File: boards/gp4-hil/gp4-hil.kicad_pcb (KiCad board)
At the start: 4 copper layers, 160 x 62 mm, 450 parts, among them J1 BEL_FUSE_0826-1G1T-23-F, J2 XILINX_JTAG, J3 XILINX_JTAG_ICESIDE, J4 XILINX_JTAG_ICESIDE, K1 CONN_3_PWROUT, P1 GPAK_ZIF, P2 2x10 HEADER, Q1 SSM6N58NU, Q11 SSM6N58NU, Q12 DMP2069UFY4, Q13 SSM6N58NU, Q14 SSM6N58NU, Q15 SSM6N58NU, Q16 SSM6N58NU, Q17 SSM6N58NU, Q18 SSM6N58NU, Q19 SSM6N58NU, Q20 SSM6N58NU, Q21 SSM6N58NU, Q22 DMP2069UFY4, U1 MIC2288-DFN, U10 AD9609, U11 DAC084S085, U12 DAC084S085, U13 DAC084S085, U14 DAC084S085, U15 TS3A4751, U16 TS3A4751, U17 TS3A4751, U18 TS3A4751, U19 TS3A4751, U2 XC7A100T-1FTG256C, U20 SIP32408, U21 SIP32408, U22 SIP32408, U23 SIP32408, U24 SIP32408, U25 TS3A4751, U26 TS3A4751, U27 TS3A4751, U29 TXB0104RUT, U3 LTC3374-QFN, U30 TXB0104RUT, U31 ADA4937-2, U32 SIP32408, U33 125 MHz, U34 INA199A2RSW, U35 INA199A2RSW, U36 INA199A2RSW, U4 SIP32408, U5 KSZ9031RN, U6 W25Q32FW, U7 25 MHz, U8 ADG726, U9 AD9609

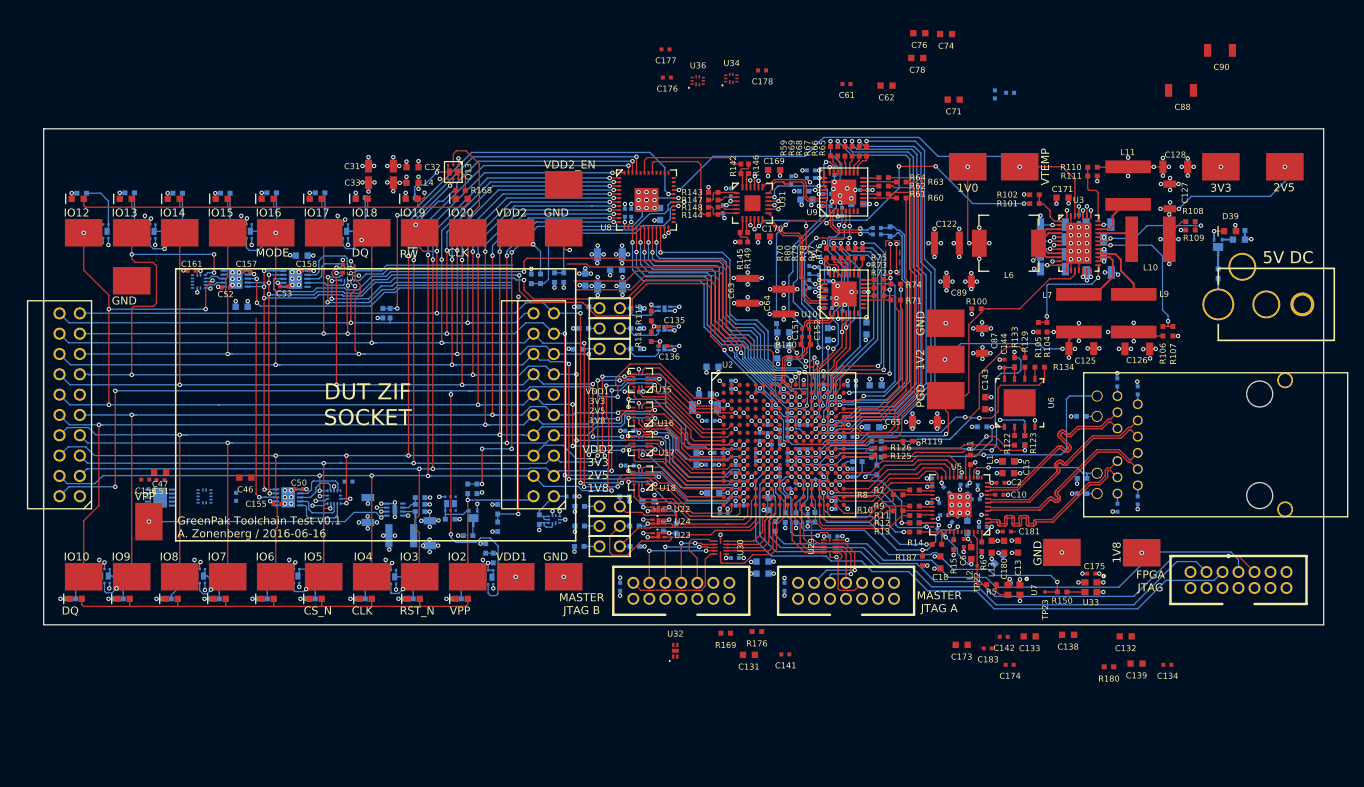
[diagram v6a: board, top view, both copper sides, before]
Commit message: Continued routing test board. 109 nets left.
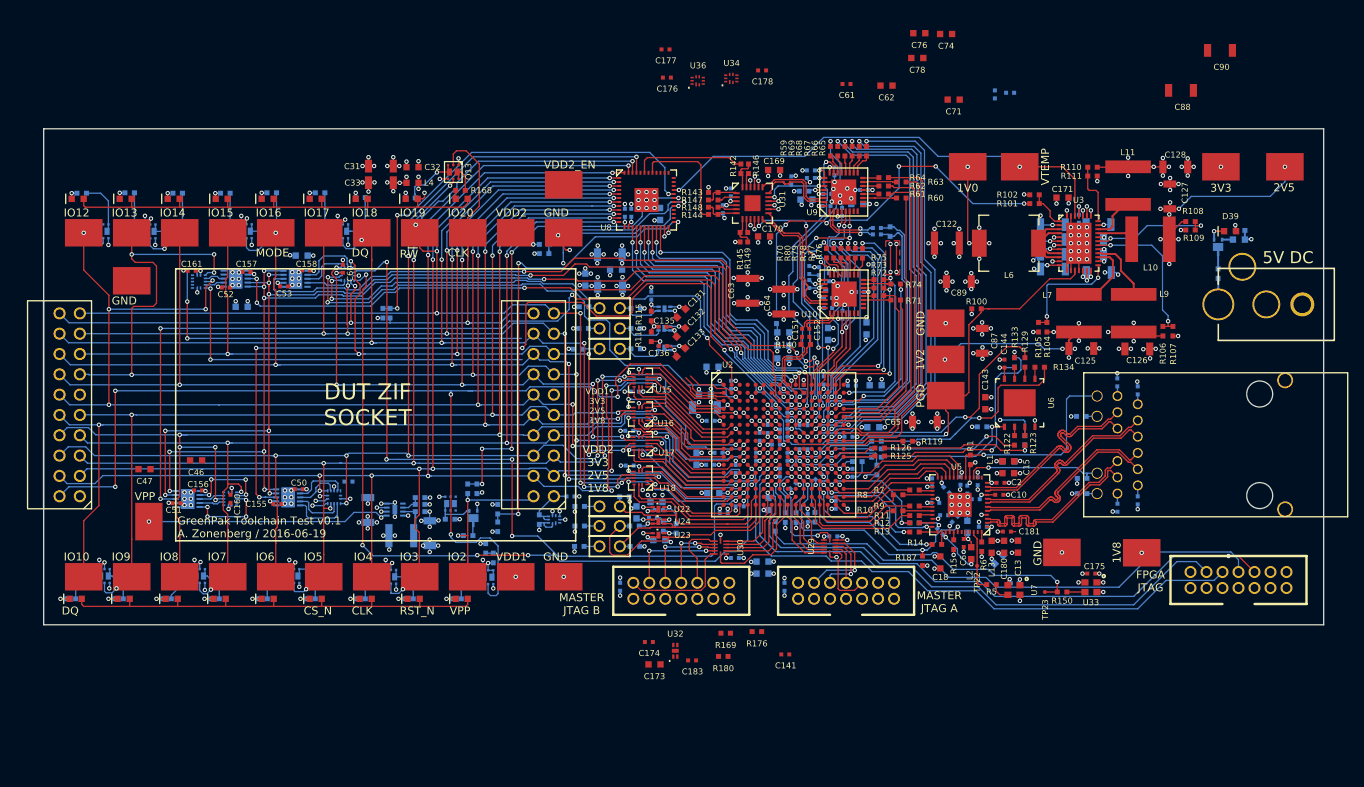
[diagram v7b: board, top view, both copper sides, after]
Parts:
- C134, C138, C139, C142: moved to B.Cu
- C160: moved to F.Cu
- moved C134 79.3 mm to (97.0, 78.8), turned to 90 degrees
- moved C132 67.3 mm to (100.7, 83.5), turned to 225 degrees
- moved C139 65.3 mm to (95.1, 106.0), turned to 90 degrees
- moved C133 56.2 mm to (100.7, 86.0), turned to 225 degrees
- moved C138 52.5 mm to (98.0, 109.4), turned to 180 degrees
- moved R180 48.2 mm to (106.0, 124.0)
- moved C142 46.3 mm to (97.2, 106.7), turned to 180 degrees
- moved C174 45.2 mm to (96.7, 122.2)
- moved C131 43.5 mm to (100.7, 81.0), turned to 225 degrees
- moved C173 38.5 mm to (97.3, 125.0)
- moved C183 37.0 mm to (102.0, 124.5)
- moved C156 6.74 mm to (40.3, 103.2), turned to 180 degrees
- moved C46 6.51 mm to (40.0, 99.5)
- moved R23 5.33 mm to (86.5, 71.3), turned to 0 degrees
- moved R19 4.62 mm to (86.5, 72.3), turned to 180 degrees
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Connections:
- U2 pad C8: /Analog IO/DAC_C_DIN -> /Analog IO/DAC_SYNC_N
- U2 pad D8: /Analog IO/DAC_SCLK -> /Analog IO/DAC_B_DIN
- U2 pad D9: /Analog IO/DAC_B_DIN -> /Analog IO/DAC_SCLK
- U2 pad E11: /Analog IO/DAC_A_DIN -> /Analog IO/DAC_C_DIN
- U2 pad G11: /Analog IO/DAC_SYNC_N -> /Analog IO/DAC_A_DIN
- U26 pad 1: /Analog IO/DUT_GPIO7 -> /Analog IO/DUT_GPIO9
- U26 pad 13: /Analog IO/GPIO7_AEN -> /Analog IO/GPIO9_AEN
- U26 pad 2: /Analog IO/GPIO7_ASIG -> /Analog IO/GPIO9_ASIG
- U26 pad 6: /Analog IO/GPIO9_AEN -> /Analog IO/GPIO7_AEN
- U26 pad 8: /Analog IO/DUT_GPIO9 -> /Analog IO/DUT_GPIO7
- U26 pad 9: /Analog IO/GPIO9_ASIG -> /Analog IO/GPIO7_ASIG
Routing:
- net /Digital IO/GPIO20_DIO: track 21.1 -> 96.5 mm, vias 1 -> 5
- net /Analog IO/DAC_B_DIN: track 40.2 -> 115.4 mm, vias 2 -> 5
- net /Digital IO/GPIO20_DEN: track 20.2 -> 90.6 mm, vias 0 -> 5
- net /Analog IO/A3V3: track 146.9 -> 210.6 mm, vias 26 -> 29
- net /Analog IO/GPIO13_AEN: track 0.00 -> 52.2 mm, vias 0 -> 2
- net /Analog IO/GPIO12_AEN: track 0.68 -> 48.5 mm, vias 1 -> 2
- net /Analog IO/DAC_A_DIN: track 67.4 -> 113.2 mm, vias 3 -> 5
- net /Analog IO/GND: track 1481.6 -> 1521.7 mm, vias 312 -> 322
- net /Analog IO/GPIO14_AEN: track 28.8 -> 66.9 mm, vias 2 -> 3
- net /Analog IO/GPIO17_AEN: track 27.2 -> 64.4 mm, vias 2 -> 3
- net /Analog IO/ADC_VPP: track 30.7 -> 58.1 mm, vias 2 -> 3
- net /Analog IO/DAC_SCLK: track 113.2 -> 131.9 mm, vias 7 -> 10
- net /Analog IO/DAC_SYNC_N: track 122.0 -> 135.8 mm, vias 7 -> 8
- net /Analog IO/DUT_GPIO8: track 141.2 -> 153.6 mm, vias 6 -> 9
- net /Analog IO/GPIO7_ASIG: track 0.00 -> 10.7 mm, vias 0 -> 4
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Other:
- board text added: "GreenPak Toolchain Test v0.1 A. Zonenberg / 2016-06-19"
- board text removed: "GreenPak Toolchain Test v0.1 A. Zonenberg / 2016-06-16"

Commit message: Continued work on test board. 77 unrouted...
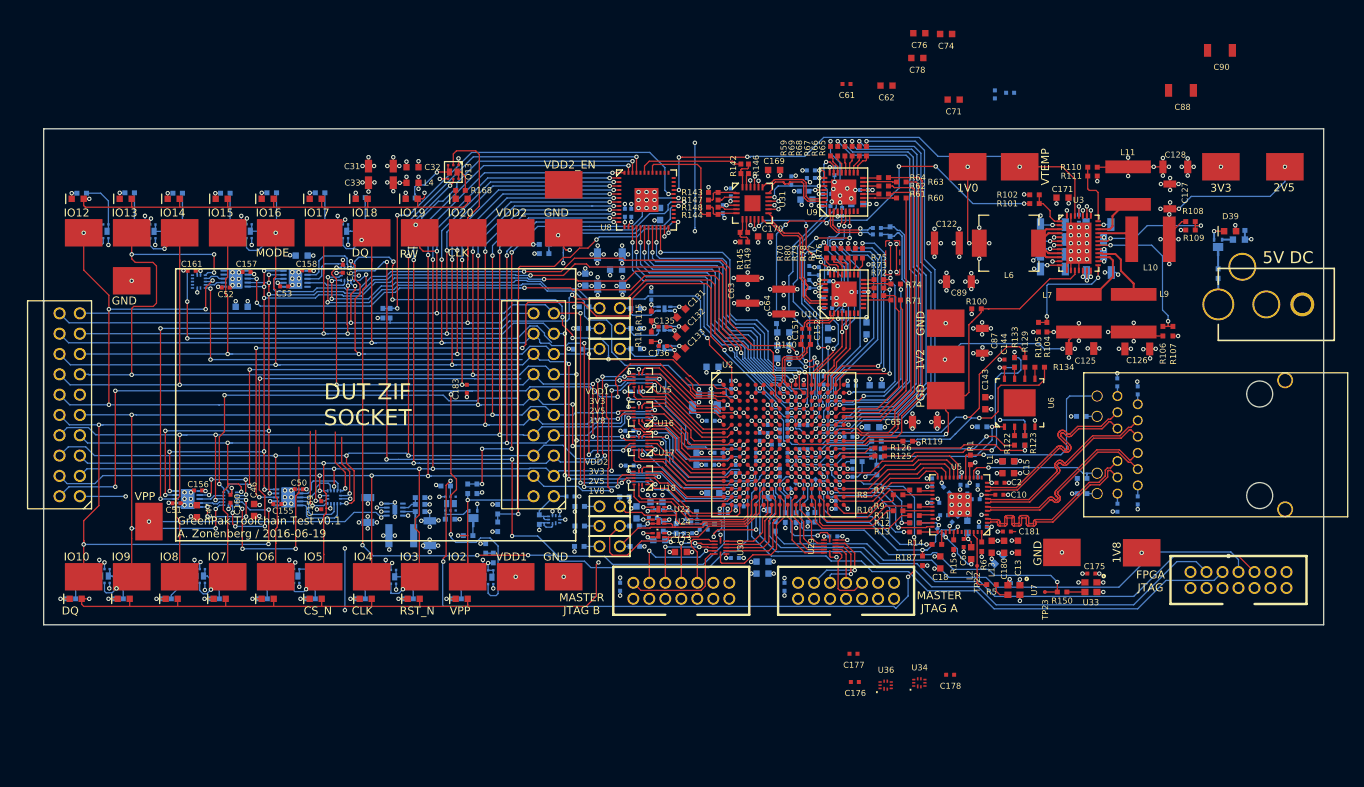
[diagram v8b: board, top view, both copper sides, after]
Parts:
- C141, C174, R169, R176, R180, U32: moved to B.Cu
- C159: moved to F.Cu
- moved C176 79.1 mm to (122.4, 127.2)
- moved C177 79.1 mm to (122.2, 123.6)
- moved C178 79.1 mm to (134.3, 126.2)
- moved U34 79.1 mm to (130.4, 127.2)
- moved U36 79.1 mm to (126.2, 127.5)
- moved C183 44.1 mm to (73.9, 90.5), turned to 270 degrees
- moved R176 42.9 mm to (71.2, 102.7)
- moved C141 19.4 mm to (101.5, 108.5)
- moved R180 16.7 mm to (104.2, 107.3), turned to 180 degrees
- moved U32 16.3 mm to (102.0, 107.1), turned to 90 degrees
- moved R169 15.8 mm to (102.0, 105.8)
- moved C174 15.6 mm to (103.5, 108.1), turned to 180 degrees
- moved C173 14.4 mm to (100.7, 110.9), turned to 180 degrees
- moved C46 9.54 mm to (47.3, 105.7), turned to 90 degrees
- moved C47 8.39 mm to (40.1, 105.8), turned to 90 degrees
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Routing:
- net /Power supply/5V0: track 111.1 -> 305.4 mm, vias 33 -> 35
- net /Analog IO/3V3: track 270.5 -> 376.2 mm, vias 17 -> 22
- net /Ethernet + JTAG/VPP_EN: track 0.71 -> 102.6 mm, vias 1 -> 5
- net /Analog IO/GPIO9_AEN: track 0.00 -> 58.0 mm, vias 0 -> 4
- net /Analog IO/GPIO15_AEN: track 6.02 -> 61.2 mm, vias 0 -> 5
- net /Analog IO/GPIO7_AEN: track 0.00 -> 51.9 mm, vias 0 -> 2
- net /Analog IO/GPIO8_AEN: track 7.58 -> 57.4 mm, vias 0 -> 2
- net /Analog IO/A3V3: track 210.6 -> 248.9 mm, vias 29 -> 31
- net /Analog IO/DUT_GPIO10: track 139.9 -> 172.2 mm, vias 6 -> 9
- net /Analog IO/GPIO10_AEN: track 5.85 -> 31.3 mm, vias 0 -> 3
- net /Analog IO/GND: track 1521.7 -> 1545.6 mm, vias 322 -> 329
- net /DUT/DUT_VDD2_EN: track 0.00 -> 19.2 mm, vias 0 -> 3
- net /Analog IO/DUT_GPIO9: track 138.0 -> 152.0 mm, vias 6 -> 9
- net /Analog IO/GPIO5_AEN: track 2.00 -> 11.4 mm
- net /Analog IO/GPIO4_AEN: track 1.60 -> 10.4 mm
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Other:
- board text removed: "DUT load switches"
